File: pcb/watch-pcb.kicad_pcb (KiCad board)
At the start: 4 copper layers, 42 x 42 mm, 71 parts, among them J1 ESP_ANT, J1 USB_C_Receptacle, J2 ESP_ANT, J2 MOTOR, J4 MOTOR, J5 Micro_SD_Card, J6 ESP_ANT, J7 USB_C_Receptacle, Q1 MBT2222ADW1T1, U1 DRV2605LYZFR, U10 APS12808L-3OBMx, U11 LSM6DSV16XTR, U12 ESP32-S3, U13 ADP2108AUJ-1.8, U14 CP2102N-Axx-xQFN28, U16 BQ25638, U17 ADP2108AUJ-1.8, U2 ESP32-S3, U2 TPS63021, U3 BQ25638, U3 TPS63021, U4 TPS65631W, U5 BQ27427YZFR, U5 ESP32-S3, U6 BQ27427YZFR, U6 TCA9535MRGER, U7 MAX30102, U8 LIS3MDL, U9 MX25LM51245GXDI00, Y1 40MHz(10ppm), Y2 32.768kHz, Y3 40MHz(10ppm), Y4 32.768kHz, Y5 40MHz(10ppm), Y6 32.768kHz

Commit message: finished pcb layout
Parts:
- removed BT2: Battery, custom-lib:Battery_Connector
- removed C100, C102: 1.5pF, Capacitor_SMD:C_0201_0603Metric
- removed the D1 at (211.7, 80.8)
- removed the D1 at (130.5, 50.5)
- removed the J1 at (130.2, 48.5)
- removed the J1 at (189.5, 72.8)
- removed the J2 at (205.8, 95.2)
- removed the J2 at (155.0, 42.0)
- removed the J5 at (134.3, 63.6)
- removed the J5 at (176.7, 87.9)
- removed J7: USB_C_Receptacle, Connector_USB:USB_C_Receptacle_GCT_USB4105-xx-A_16P_TopMnt_Horizontal
- removed JP2, JP3, JP4, JP5, JP8: GP6, Jumper:SolderJumper-3_P1.3mm_Open_RoundedPad1.0x1.5mm
- removed JP6, JP7: RESET=LOW, Jumper:SolderJumper-2_P1.3mm_Open_RoundedPad1.0x1.5mm
- removed L13: 2.7nH, Inductor_SMD:L_0201_0603Metric
- removed the MK1 at (204.6, 101.0)
- removed the MK1 at (161.7, 67.0)
- removed R57: R, PCM_Resistor_SMD_AKL:R_0402_1005Metric
- removed the U1 at (199.7, 101.7)
- removed the U1 at (147.5, 76.0)
- removed the U10 at (182.2, 75.1)
- removed the U10 at (147.0, 41.0)
- removed the U11 at (204.6, 105.5)
- removed the U11 at (146.0, 57.0)
- removed U16: BQ25638, custom-lib:Texas_DSBGA-30_2.0x2.4mm_Layout5x6_P0.4mm
- removed U17: ADP2108AUJ-1.8, Package_TO_SOT_SMD:TSOT-23-5
- removed the U2 at (145.5, 62.4)
- removed the U2 at (188.8, 85.0)
- removed the U3 at (207.7, 83.1)
- removed the U3 at (140.7, 55.5)
- removed the U4 at (164.2, 56.6)
- removed the U4 at (209.3, 105.5)
- removed the U5 at (215.2, 82.1)
- removed the U5 at (152.8, 49.0)
- removed the U6 at (127.5, 56.5)
- removed the U6 at (187.3, 92.8)
- removed the U7 at (199.9, 95.8)
- removed the U7 at (146.0, 57.0)
- removed the U8 at (154.2, 59.2)
- removed the U8 at (199.3, 105.7)
- removed the U9 at (173.6, 75.1)
- removed the U9 at (147.0, 41.0)
- removed Y3, Y5: 40MHz(10ppm), Crystal:Crystal_SMD_3225-4Pin_3.2x2.5mm
- removed Y4, Y6: 32.768kHz, Crystal:Crystal_SMD_3215-2Pin_3.2x1.5mm
- added C1: 10uF, Capacitor_SMD:C_0603_1608Metric, B.Cu at (114.3, 83.2)
- added C10: 22uF, Capacitor_SMD:C_0603_1608Metric, F.Cu at (113.2, 76.4)
- added C11: 1uF, Capacitor_SMD:C_0402_1005Metric, F.Cu at (110.3, 53.2)
- added C12: 100nF, Capacitor_SMD:C_0402_1005Metric, B.Cu at (130.7, 78.0)
- added C13: 10uF, Capacitor_SMD:C_0402_1005Metric, B.Cu at (131.7, 78.0)
- added C14: 22uF, Capacitor_SMD:C_0603_1608Metric, B.Cu at (108.3, 56.8)
- added C15: 2.2uF, Capacitor_SMD:C_0402_1005Metric, F.Cu at (113.3, 55.5)
- added C16: 22uF, Capacitor_SMD:C_0603_1608Metric, B.Cu at (110.0, 58.6)
- added C17: 22uF, Capacitor_SMD:C_0603_1608Metric, B.Cu at (106.6, 55.0)
- added C18: 1uF, Capacitor_SMD:C_0402_1005Metric, B.Cu at (108.2, 63.6)
- added C19: 10uF, Capacitor_SMD:C_0402_1005Metric, B.Cu at (107.4, 65.7)
- added C2: 10uF, Capacitor_SMD:C_0603_1608Metric, B.Cu at (114.3, 81.7)
- added C20: 4.7uF, Capacitor_SMD:C_0402_1005Metric, F.Cu at (108.0, 67.8)
- added C21: 4.7uF, Capacitor_SMD:C_0402_1005Metric, F.Cu at (111.7, 64.4)
- added C22: 47nF, Capacitor_SMD:C_0402_1005Metric, F.Cu at (108.7, 66.7)
- added C23: 10uF, Capacitor_SMD:C_0603_1608Metric, B.Cu at (109.9, 62.6)
- added C24: 10uF, Capacitor_SMD:C_0603_1608Metric, B.Cu at (111.4, 62.6)
- added C25: 1.5pF, Capacitor_SMD:C_0201_0603Metric, F.Cu at (121.6, 52.5)
- added C26: 1uF, Capacitor_SMD:C_0402_1005Metric, B.Cu at (120.2, 54.0)
- added C27: C, Capacitor_SMD:C_0402_1005Metric, F.Cu at (114.0, 57.0)
- added C28: C, Capacitor_SMD:C_0402_1005Metric, F.Cu at (114.0, 63.0)
- added C29: 1.5pF, Capacitor_SMD:C_0201_0603Metric, F.Cu at (122.0, 55.5)
- added C3: 4.7uF, Capacitor_SMD:C_0402_1005Metric, B.Cu at (113.7, 59.8)
- added C30: 100nF, Capacitor_SMD:C_0402_1005Metric, B.Cu at (123.0, 67.2)
- added C31: 1uF, Capacitor_SMD:C_0402_1005Metric, F.Cu at (123.2, 72.5)
- added C32: 100nF, Capacitor_SMD:C_0402_1005Metric, B.Cu at (115.7, 59.6)
- added C33: 1uF, Capacitor_SMD:C_0402_1005Metric, F.Cu at (124.8, 55.5)
- added C34: 1uF, Capacitor_SMD:C_0402_1005Metric, B.Cu at (115.0, 63.8)
- added C35: 100nF, Capacitor_SMD:C_0402_1005Metric, F.Cu at (123.8, 61.6)
- added C36: 10nF, Capacitor_SMD:C_0402_1005Metric, F.Cu at (123.5, 55.5)
- added C37: 100nF, Capacitor_SMD:C_0402_1005Metric, B.Cu at (115.0, 64.8)
- added C38: 100nF, Capacitor_SMD:C_0402_1005Metric, B.Cu at (121.3, 56.8)
- added C39: 100nF, Capacitor_SMD:C_0402_1005Metric, B.Cu at (125.3, 54.9)
- added C4: 100nF, Capacitor_SMD:C_0603_1608Metric, B.Cu at (110.3, 78.5)
- added C40: 1uF, Capacitor_SMD:C_0402_1005Metric, B.Cu at (125.5, 53.8)
- added C41: C, Capacitor_SMD:C_0402_1005Metric, F.Cu at (127.3, 56.5)
- added C42: C, Capacitor_SMD:C_0402_1005Metric, F.Cu at (127.2, 61.7)
- added C43: 10uF, Capacitor_SMD:C_0402_1005Metric, B.Cu at (123.8, 53.0)
- added C44: 10uF, Capacitor_SMD:C_0402_1005Metric, B.Cu at (122.5, 53.0)
- added C45: 10uF, Capacitor_SMD:C_0402_1005Metric, B.Cu at (100.9, 80.6)
- added C46: 100nF, Capacitor_SMD:C_0402_1005Metric, F.Cu at (126.7, 63.3)
- added C47: 1uF, Capacitor_SMD:C_0402_1005Metric, F.Cu at (128.9, 62.7)
- added C48: 100nF, Capacitor_SMD:C_0402_1005Metric, B.Cu at (131.2, 58.8)
- added C49: 10uF, Capacitor_SMD:C_0402_1005Metric, F.Cu at (129.9, 58.7)
- added C5: 10nF, Capacitor_SMD:C_0402_1005Metric, B.Cu at (107.3, 62.3)
- added C50: 100nF, Capacitor_SMD:C_0402_1005Metric, F.Cu at (116.3, 84.5)
- added C51: 100nF, Capacitor_SMD:C_0402_1005Metric, B.Cu at (120.3, 86.6)
- added C52: 10uF, Capacitor_SMD:C_0402_1005Metric, F.Cu at (117.3, 84.5)
- added C53: 1uF, Capacitor_SMD:C_0402_1005Metric, B.Cu at (119.2, 87.6)
- added C54: 100nF, Capacitor_SMD:C_0402_1005Metric, F.Cu at (119.5, 72.7)
- added C55: 10uF, Capacitor_SMD:C_0402_1005Metric, F.Cu at (121.0, 73.9)
- added C56: 1uF, Capacitor_SMD:C_0402_1005Metric, B.Cu at (121.7, 91.5)
- added C57: 100nF, Capacitor_SMD:C_0402_1005Metric, F.Cu at (117.6, 69.8)
- added C58: 4.7uF, Capacitor_SMD:C_0402_1005Metric, F.Cu at (117.6, 68.8)
- added C59: 1uF, Capacitor_SMD:C_0402_1005Metric, F.Cu at (119.4, 73.9)
- added C6: 10uF, Capacitor_SMD:C_0402_1005Metric, B.Cu at (111.2, 55.2)
- added C60: 100nF, Capacitor_SMD:C_0402_1005Metric, F.Cu at (115.6, 73.9)
- added C61: 100nF, Capacitor_SMD:C_0402_1005Metric, F.Cu at (117.5, 73.9)
- added C62: 10uF, Capacitor_SMD:C_0402_1005Metric, F.Cu at (114.0, 84.0)
- added C63: 10uF, Capacitor_SMD:C_0402_1005Metric, F.Cu at (117.9, 90.1)
- added C64: 1uF, Capacitor_SMD:C_0402_1005Metric, F.Cu at (108.3, 85.8)
- added C65: 100nF, Capacitor_SMD:C_0402_1005Metric, F.Cu at (109.8, 85.1)
- added C66: 1uF, Capacitor_SMD:C_0402_1005Metric, B.Cu at (114.4, 87.7)
- added C67: 100nF, Capacitor_SMD:C_0402_1005Metric, F.Cu at (114.4, 87.7)
- added C68: 100nF, Capacitor_SMD:C_0402_1005Metric, F.Cu at (99.0, 72.6)
- added C69: 1uF, Capacitor_SMD:C_0402_1005Metric, F.Cu at (100.6, 71.9)
- added C7: 22uF, Capacitor_SMD:C_0603_1608Metric, F.Cu at (113.2, 72.9)
- added C72: 100nF, Capacitor_SMD:C_0402_1005Metric, B.Cu at (108.0, 86.5)
- added C73: 100nF, Capacitor_SMD:C_0402_1005Metric, F.Cu at (109.5, 88.0)
- added C74: 100nF, Capacitor_SMD:C_0402_1005Metric, F.Cu at (132.9, 73.0)
- added C75: 1uF, Capacitor_SMD:C_0402_1005Metric, F.Cu at (131.9, 73.0)
- added C76: 100nF, Capacitor_SMD:C_0402_1005Metric, F.Cu at (129.7, 64.3)
- added C77: 100nF, Capacitor_SMD:C_0402_1005Metric, F.Cu at (128.9, 67.4)
- added C78: 100nF, Capacitor_SMD:C_0402_1005Metric, F.Cu at (125.4, 72.5)
- added C79: 100nF, Capacitor_SMD:C_0402_1005Metric, B.Cu at (123.0, 66.2)
- added C8: 22uF, Capacitor_SMD:C_0603_1608Metric, F.Cu at (113.2, 74.7)
- added C9: 1uF, Capacitor_SMD:C_0402_1005Metric, B.Cu at (133.5, 80.7)
- added D1: STATUS1, LED_SMD:LED_0402_1005Metric, F.Cu at (97.0, 72.6)
- added D10: ESD9B3.3ST5G, Diode_SMD:D_SOD-923, B.Cu at (101.2, 82.0)
- added D11: ESD9B3.3ST5G, Diode_SMD:D_SOD-923, B.Cu at (101.4, 79.1)
- added D12: ESD9B3.3ST5G, Diode_SMD:D_SOD-923, B.Cu at (100.4, 78.7)
- added D13: ESD9B3.3ST5G, Diode_SMD:D_SOD-923, B.Cu at (99.1, 77.8)
- added D14: ESD9B3.3ST5G, Diode_SMD:D_SOD-923, B.Cu at (99.4, 81.7)
- added D15: STATUS0, LED_SMD:LED_0402_1005Metric, F.Cu at (97.4, 68.1)
- added D6: CHARGING, LED_SMD:LED_0402_1005Metric, B.Cu at (105.8, 63.5)
- added D7: POWER GOOD, LED_SMD:LED_0402_1005Metric, B.Cu at (105.8, 64.5)
- added D8: ESD9B3.3ST5G, Diode_SMD:D_SOD-923, B.Cu at (101.2, 84.1)
- added J1: DAUGHTER, Connector_FFC-FPC:TE_1-1734839-2_1x12-1MP_P0.5mm_Horizontal, F.Cu at (133.6, 65.3)
- added J2: USB_C_Receptacle, Connector_USB:USB_C_Receptacle_GCT_USB4105-xx-A_16P_TopMnt_Horizontal, F.Cu at (101.0, 62.8)
- added J3: ESP_ANT, Connector_Coaxial:U.FL_Molex_MCRF_73412-0110_Vertical, F.Cu at (118.5, 53.5)
- added J5: ELV1411A, custom-lib:ELV1411A, F.Cu at (126.8, 81.7)
- added L1: 1.5uH, custom-lib:XFL4020-152ME, F.Cu at (118.0, 76.9)
- added L2: 1uH, Inductor_SMD:L_1206_3216Metric, B.Cu at (113.8, 52.8)
- added L3: 1uH, Inductor_SMD:L_1206_3216Metric, F.Cu at (108.7, 63.6)
- added L4: 2.7nH, Inductor_SMD:L_0201_0603Metric, F.Cu at (121.6, 54.2)
- added L5: 2nH, Inductor_SMD:L_0805_2012Metric, B.Cu at (123.2, 55.9)
- added L6: 24nH, Inductor_SMD:L_Coilcraft_XFL2010, F.Cu at (124.2, 58.0)
- added L8: 10uH, Inductor_SMD:L_1008_2520Metric, B.Cu at (115.2, 89.8)
- added MK1: ICS-43434, Sensor_Audio:InvenSense_ICS-43434-6_3.5x2.65mm, F.Cu at (97.9, 70.4)
- added Q2: MMBT3904, Package_TO_SOT_SMD:SOT-23, B.Cu at (122.6, 81.6)
- added Q3: MMBT3904, Package_TO_SOT_SMD:SOT-23, B.Cu at (126.0, 87.1)
- added Q4: MMBT3904, Package_TO_SOT_SMD:SOT-23, B.Cu at (124.3, 77.8)
- added Q5: MMBT3904, Package_TO_SOT_SMD:SOT-23, B.Cu at (122.6, 85.6)
- added Q6: MMBT3904, Package_TO_SOT_SMD:SOT-23, B.Cu at (118.7, 80.4)
- added R1: 10k, Resistor_SMD:R_0402_1005Metric, F.Cu at (107.8, 28.3)
- added R10: 10k, Resistor_SMD:R_0402_1005Metric, F.Cu at (115.6, 33.9)
- added R11: 5.1k, Resistor_SMD:R_0402_1005Metric, F.Cu at (106.9, 64.0)
- added R12: 5.1k, Resistor_SMD:R_0402_1005Metric, F.Cu at (105.0, 67.4)
- added R13: 180k, Resistor_SMD:R_0402_1005Metric, F.Cu at (110.8, 74.0)
- added R14: 1M, Resistor_SMD:R_0402_1005Metric, F.Cu at (110.2, 72.2)
- added R15: 1M, Resistor_SMD:R_0402_1005Metric, B.Cu at (110.3, 80.7)
- added R16: 22.1k, Resistor_SMD:R_0402_1005Metric, F.Cu at (132.8, 75.7)
- added R17: 47.5k, Resistor_SMD:R_0402_1005Metric, F.Cu at (134.3, 76.8)
- added R18: 1k, Resistor_SMD:R_0402_1005Metric, B.Cu at (133.5, 81.7)
- added R19: 10k, Resistor_SMD:R_0402_1005Metric, F.Cu at (114.8, 52.0)
- added R2: 10k, Resistor_SMD:R_0402_1005Metric, F.Cu at (107.8, 30.3)
- added R20: 0, Resistor_SMD:R_0402_1005Metric, B.Cu at (125.3, 81.0)
- added R22: 30.31, Resistor_SMD:R_0402_1005Metric, B.Cu at (112.8, 63.1)
- added R23: 2222, Resistor_SMD:R_0402_1005Metric, B.Cu at (121.4, 79.1)
- added R24: 10k, Resistor_SMD:R_0402_1005Metric, B.Cu at (125.8, 83.5)
- added R25: 10k, Resistor_SMD:R_0402_1005Metric, B.Cu at (125.3, 80.0)
- added R26: 5.24k, Resistor_SMD:R_0402_1005Metric, B.Cu at (112.8, 65.1)
- added R27: 6666, Resistor_SMD:R_0402_1005Metric, B.Cu at (119.9, 85.1)
- added R28: 0, Resistor_SMD:R_0402_1005Metric, F.Cu at (122.6, 75.7)
- added R29: 0, Resistor_SMD:R_0402_1005Metric, F.Cu at (135.4, 78.3)
- added R3: R, Resistor_SMD:R_0402_1005Metric, F.Cu at (98.0, 73.6)
- added R30: 33k, Resistor_SMD:R_0402_1005Metric, B.Cu at (119.9, 84.1)
- added R31: 10k, Resistor_SMD:R_0402_1005Metric, B.Cu at (121.2, 54.0)
- added R32: 10k, Resistor_SMD:R_0402_1005Metric, B.Cu at (120.7, 55.5)
- added R33: 499, Resistor_SMD:R_0402_1005Metric, B.Cu at (122.9, 60.5)
- added R34: 0, Resistor_SMD:R_0402_1005Metric, F.Cu at (114.3, 65.3)
- added R35: 0, Resistor_SMD:R_0402_1005Metric, F.Cu at (115.3, 65.3)
- added R36: 0, Resistor_SMD:R_0402_1005Metric, F.Cu at (116.3, 65.3)
- added R37: 0, Resistor_SMD:R_0402_1005Metric, F.Cu at (117.3, 65.3)
- added R38: 0, Resistor_SMD:R_0402_1005Metric, F.Cu at (118.3, 65.3)
- added R39: R, PCM_Resistor_SMD_AKL:R_0402_1005Metric, F.Cu at (111.5, 60.0)
- added R4: 10k, Resistor_SMD:R_0402_1005Metric, F.Cu at (107.8, 34.3)
- added R40: 10k, Resistor_SMD:R_0402_1005Metric, F.Cu at (129.3, 69.3)
- added R41: 0, Resistor_SMD:R_0402_1005Metric, B.Cu at (118.9, 64.5)
- added R42: 0, Resistor_SMD:R_0402_1005Metric, B.Cu at (119.9, 64.5)
- added R43: 0, Resistor_SMD:R_0402_1005Metric, B.Cu at (120.9, 64.5)
- added R44: 0, Resistor_SMD:R_0402_1005Metric, B.Cu at (121.9, 64.5)
- added R45: 0, Resistor_SMD:R_0402_1005Metric, F.Cu at (123.9, 63.9)
- added R46: 10k, Resistor_SMD:R_0402_1005Metric, B.Cu at (103.0, 84.1)
- added R47: 10k, Resistor_SMD:R_0402_1005Metric, B.Cu at (102.5, 83.1)
- added R48: 10k, Resistor_SMD:R_0402_1005Metric, B.Cu at (103.0, 82.0)
- added R49: 10k, Resistor_SMD:R_0402_1005Metric, B.Cu at (102.4, 80.2)
- added R5: 10k, Resistor_SMD:R_0402_1005Metric, F.Cu at (107.8, 36.3)
- added R50: 10k, Resistor_SMD:R_0402_1005Metric, B.Cu at (100.4, 76.9)
- added R51: 10k, Resistor_SMD:R_0402_1005Metric, B.Cu at (99.1, 76.0)
- added R52: 10k, Resistor_SMD:R_0402_1005Metric, B.Cu at (134.0, 64.3)
- added R53: 10k, Resistor_SMD:R_0402_1005Metric, F.Cu at (131.2, 58.1)
- added R54: 10k, Resistor_SMD:R_0402_1005Metric, F.Cu at (102.7, 70.7)
- added R55: R, Resistor_SMD:R_0402_1005Metric, F.Cu at (103.9, 69.6)
- added R6: 10k, Resistor_SMD:R_0402_1005Metric, F.Cu at (111.0, 30.9)
- added R7: 10k, Resistor_SMD:R_0402_1005Metric, F.Cu at (111.0, 32.9)
- added R8: 10k, Resistor_SMD:R_0402_1005Metric, F.Cu at (111.0, 34.9)
- added R9: 10k, Resistor_SMD:R_0402_1005Metric, F.Cu at (115.6, 31.9)
- added TH1: 103AT-2 10k, Resistor_THT:R_Axial_DIN0204_L3.6mm_D1.6mm_P2.54mm_Vertical, F.Cu at (113.2, 68.2)
- added TP1: MTP_PWR, TestPoint:TestPoint_Pad_D1.0mm, B.Cu at (112.7, 85.2)
- added U1: ADP2108AUJ-1.8, Package_TO_SOT_SMD:TSOT-23-5, B.Cu at (113.7, 56.4)
- added U10: MAX30102, OptoDevice:Maxim_OLGA-14_3.3x5.6mm_P0.8mm, B.Cu at (116.8, 71.8)
- added U11: TPS65631W, Package_SON:WSON-10-1EP_2.5x2.5mm_P0.5mm_EP1.2x2mm_ThermalVias, F.Cu at (117.5, 87.5)
- added U2: TPS63021, custom-lib:Texas_VSON-14_3x4mm_ThermalPad, B.Cu at (114.2, 78.9)
- added U3: CP2102N-Axx-xQFN28, Package_DFN_QFN:QFN-28-1EP_5x5mm_P0.5mm_EP3.35x3.35mm, B.Cu at (129.4, 82.1)
- added U4: BQ27427YZFR, Package_BGA:Texas_DSBGA-9_1.4715x1.4715mm_Layout3x3_P0.5mm, F.Cu at (112.5, 53.2)
- added U5: BQ25638, custom-lib:Texas_DSBGA-30_2.0x2.4mm_Layout5x6_P0.4mm, B.Cu at (109.8, 65.7)
- added U6: ESP32-S3, Package_DFN_QFN:QFN-56-1EP_7x7mm_P0.4mm_EP4x4mm_ThermalVias, F.Cu at (118.8, 60.2)
- added U7: MX25LM51245GXDI00, custom-lib:BGA-24_6.0x8.0mm_Layout5x5_P1.0mm, F.Cu at (123.6, 68.2)
- added U8: APS12808L-3OBMx, custom-lib:BGA-24_6.0x8.0mm_Layout5x5_P1.0mm, B.Cu at (128.7, 64.8)
- added U9: TCA9535MRGER, Package_DFN_QFN:VQFN-24-1EP_4x4mm_P0.5mm_EP2.45x2.45mm, B.Cu at (127.8, 58.3)
- C70: value 1.5pF -> 1uF; footprint Capacitor_SMD:C_0201_0603Metric -> Capacitor_SMD:C_0402_1005Metric; moved to B.Cu
- C71: value 1.5pF -> 100nF; footprint Capacitor_SMD:C_0201_0603Metric -> Capacitor_SMD:C_0402_1005Metric
- D2, D3: moved to B.Cu
- D4, D5: value ESD9B3.3ST5G -> ESD9B5.0ST5G
- D9: value ESD9B5.0ST5G -> ESD9B3.3ST5G; moved to B.Cu
- J4: value MOTOR -> Micro_SD_Card; footprint custom-lib:Battery_Connector -> Connector_Card:microSD_HC_Hirose_DM3D-SF
- J6: value ESP_ANT -> TT143AMC12C; footprint Connector_Coaxial:U.FL_Molex_MCRF_73412-0110_Vertical -> custom-lib:OK-14GF024-04
- JP1: value BOOT -> RESET=LOW; moved to F.Cu
- L7: value 2.7nH -> 10uH; footprint Inductor_SMD:L_0201_0603Metric -> Inductor_SMD:L_1008_2520Metric; moved to B.Cu
- Q1: value MBT2222ADW1T1 -> MMBT3904; footprint Package_TO_SOT_SMD:SOT-363_SC-70-6 -> Package_TO_SOT_SMD:SOT-23; moved to B.Cu
- R21: value R -> 0; footprint PCM_Resistor_SMD_AKL:R_0402_1005Metric -> Resistor_SMD:R_0402_1005Metric; moved to B.Cu
- U12: value ESP32-S3 -> DRV2605LYZFR; footprint Package_DFN_QFN:QFN-56-1EP_7x7mm_P0.4mm_EP4x4mm_ThermalVias -> Package_BGA:Texas_DSBGA-9_1.4715x1.4715mm_Layout3x3_P0.5mm; moved to B.Cu
- U13: value ADP2108AUJ-1.8 -> LSM6DSV16XTR; footprint Package_TO_SOT_SMD:TSOT-23-5 -> Package_LGA:LGA-14_3x2.5mm_P0.5mm_LayoutBorder3x4y
- U14: value CP2102N-Axx-xQFN28 -> LIS3MDL; footprint Package_DFN_QFN:QFN-28-1EP_5x5mm_P0.5mm_EP3.35x3.35mm -> Package_LGA:LGA-12_2x2mm_P0.5mm
- Y1: value 40MHz(10ppm) -> 32.768kHz; footprint Crystal:Crystal_SMD_3225-4Pin_3.2x2.5mm -> Crystal:Crystal_SMD_3215-2Pin_3.2x1.5mm
- Y2: value 32.768kHz -> 40MHz(10ppm); footprint Crystal:Crystal_SMD_3215-2Pin_3.2x1.5mm -> Crystal:Crystal_SMD_3225-4Pin_3.2x2.5mm
- moved D9 111.0 mm to (100.7, 83.1)
- moved D3 109.5 mm to (104.3, 63.2), turned to -90 degrees
- moved D2 107.6 mm to (105.4, 65.6), turned to 180 degrees
- moved U14 106.4 mm to (107.5, 88.5), turned to 180 degrees
- moved C71 103.3 mm to (105.5, 88.0), turned to -90 degrees
- moved C70 102.3 mm to (106.8, 86.5), turned to -90 degrees
- moved J4 96.0 mm to (104.7, 78.8), turned to -60 degrees
- moved D4 93.6 mm to (105.9, 65.1), turned to 90 degrees
- moved D5 92.9 mm to (106.2, 55.0)
- moved L7 90.2 mm to (117.5, 84.5), turned to -90 degrees
- moved J6 80.4 mm to (111.9, 88.1), turned to -90 degrees
- moved MK2 78.4 mm to (135.5, 73.7), turned to 90 degrees
- moved U12 77.7 mm to (121.4, 89.3)
- moved U13 75.0 mm to (116.8, 71.8)
- moved Q1 73.0 mm to (134.3, 78.3), turned to -90 degrees
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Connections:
- BT1 pad 1: /BAT+ -> +BATT
- C70 pad 1: Net-(J6-In) -> GND
- C70 pad 2: GND -> +3V3
- C71 pad 1: /ESP_ANT -> GND
- C71 pad 2: GND -> +3V3
- D4 pad 2: /USB_DP -> /USB and Power/USB_DM
- D5 pad 2: /USB_DM -> +BATT
- D9 pad 2: /USB and Power/USB_DM -> /MCU and Memory/SD_D3
- J4 pad 1: /MTR_P -> /MCU and Memory/SD_D2
- J4 pad 2: /MTR_M -> /MCU and Memory/SD_D3
- J6 pad 1: Net-(J6-In) -> +3V3
- J6 pad 2: GND -> /IO/TP_INT
- JP1 pad 2: /I2C0_SCL -> /MCU and Memory/EN
- L7 pad 1: Net-(J6-In) -> GND
- L7 pad 2: /ESP_ANT -> Net-(U11-SWN)
- MK2 pad 2: GND -> +3V3
- Q1 pad 1: /USB and Power/RTS -> Net-(Q1-B)
- Q1 pad 2: Net-(Q1A-B1) -> GND
- R21 pad 1: /RTC_P -> Net-(U3-RXD)
- R21 pad 2: /RTC_N -> /MCU and Memory/TX
- U13 pad 1: VBUS -> GND
- U13 pad 2: GND -> /IO/IMU_SDA
- U13 pad 3: VBUS -> /IO/IMU_SCL
- U13 pad 4: +1V8 -> /IO/IMU_INT1
- U13 pad 5: Net-(U13-SW) -> +3V3
- U14 pad 1: unconnected-(U14-~{DCD}-Pad1) -> /IO/IMU_SCL
- U14 pad 10: unconnected-(U14-NC-Pad10) -> +3V3
- U14 pad 11: unconnected-(U14-~{SUSPEND}-Pad11) -> /IO/IMU_SDA
- U14 pad 12: unconnected-(U14-SUSPEND-Pad12) -> GND
- U14 pad 2: unconnected-(U14-~{RI}/CLK-Pad2) -> GND
- U14 pad 4: /USB and Power/USB_DP -> Net-(U14-C1)
- U14 pad 5: /USB and Power/USB_DM -> +3V3
- U14 pad 7: +3V3 -> /IO/MAG_INT
- U14 pad 8: Net-(U14-VBUS) -> /IO/MAG_DRDY
- U14 pad 9: Net-(U14-~{RST}) -> GND
- Y1 pad 1: /CLK_P -> /MCU and Memory/RTC_N
- Y1 pad 2: GND -> /MCU and Memory/RTC_P
- Y2 pad 1: /RTC_N -> Net-(C41-Pad1)
- Y2 pad 2: /RTC_P -> GND
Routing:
- added copper zone on B.Cu, net GND
- added copper zone on F.Cu, net GND
- added copper zone on In1.Cu, net GND
- added copper zone on In2.Cu, net GND
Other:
- outline, holes or cut-outs redrawn

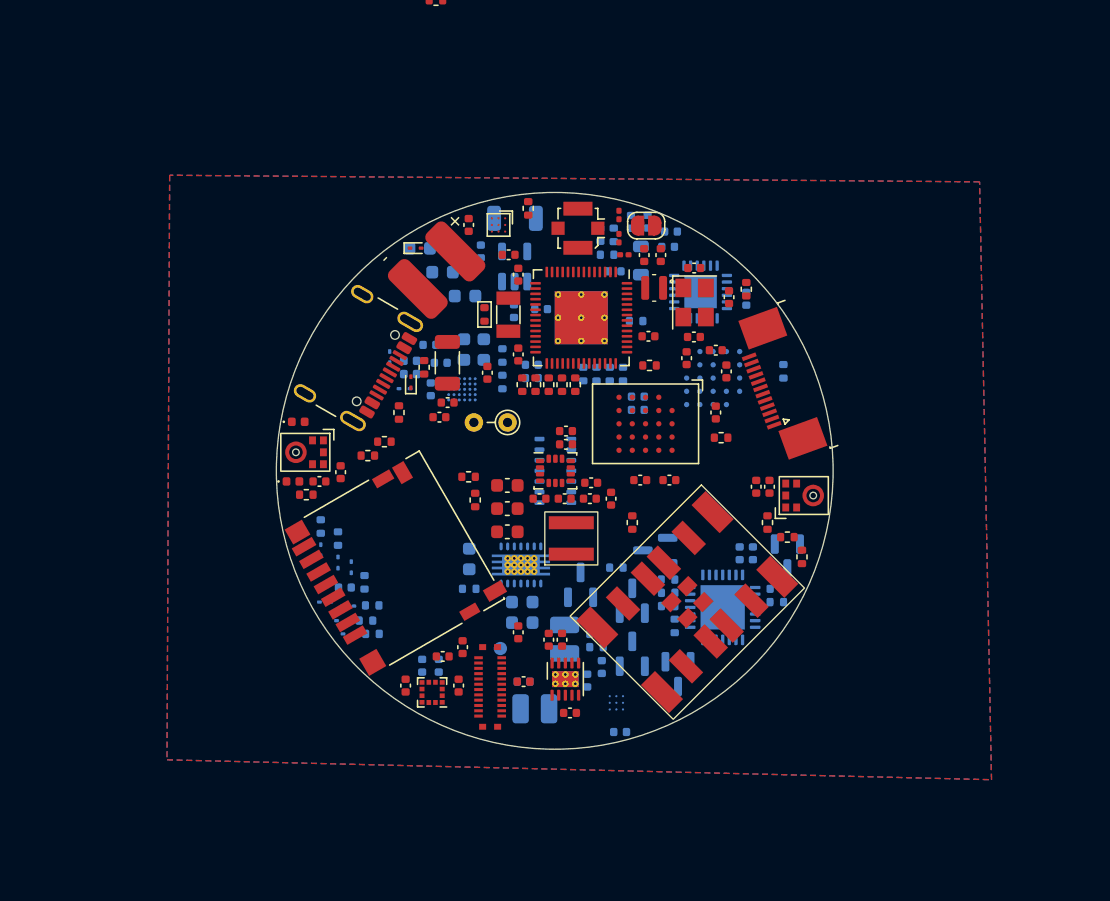
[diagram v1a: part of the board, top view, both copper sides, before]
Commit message: switching to 6 layer
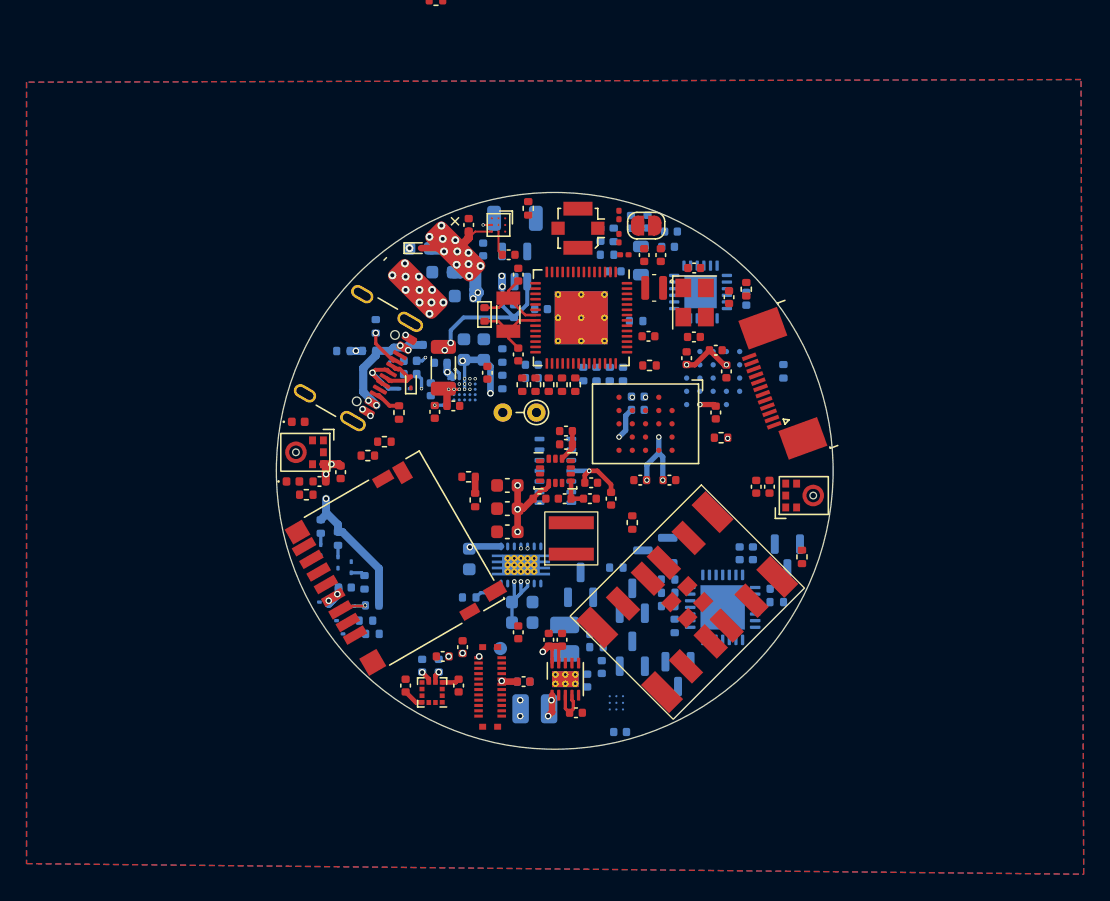
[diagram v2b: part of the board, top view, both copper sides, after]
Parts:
- R11, R16, R17: moved to B.Cu
- moved R17 36.3 mm to (100.8, 62.8), turned to 0 degrees
- moved R16 32.7 mm to (102.8, 62.8), turned to 0 degrees
- moved R11 4.78 mm to (103.2, 60.9), turned to 90 degrees
- moved TH1 2.31 mm to (115.4, 67.4)
- moved R15 0.65 mm to (110.3, 81.3)
- moved C20 0.53 mm to (107.7, 67.3), turned to 90 degrees
- moved C22 0.50 mm to (109.1, 66.9)
- moved L3 0.48 mm to (108.3, 64.0)
- moved C63 0.45 mm to (118.3, 90.0)
- moved C6 0.23 mm to (111.3, 55.1)
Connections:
- net /USB and Power/USB_DM renamed /USB and Power/USB_DN
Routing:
- net +3V3: track 0.00 -> 72.2 mm, vias 0 -> 28
- net +VSW: track 0.00 -> 54.5 mm, vias 0 -> 14
- net +BATT: track 0.00 -> 29.3 mm, vias 0 -> 17
- net VBUS: track 0.00 -> 19.6 mm, vias 0 -> 5
- net /MCU and Memory/RTC_P: track 0.00 -> 6.28 mm
- net /MCU and Memory/RTC_N: track 0.00 -> 6.09 mm
- net /USB and Power/USB_DP: track 0.00 -> 5.48 mm, vias 0 -> 1
- net +1V8: track 0.00 -> 5.05 mm, vias 0 -> 1
- net Net-(D7-K): track 0.00 -> 4.25 mm, vias 0 -> 2
- net Net-(D6-K): track 0.00 -> 4.22 mm, vias 0 -> 2
- net /USB and Power/USB_DN: track 0.00 -> 3.70 mm
- net /IO/AMOLED_P: track 0.00 -> 2.94 mm
- net Net-(J2-CC1): track 0.00 -> 2.90 mm, vias 0 -> 1
- net /MCU and Memory/SD_CMD: track 0.00 -> 2.87 mm, vias 0 -> 1
- net Net-(C22-Pad2): track 0.00 -> 2.63 mm, vias 0 -> 3
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
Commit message: made many changes, maybe switching to stm tho
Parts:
- removed C34: 1uF, Capacitor_SMD:C_0402_1005Metric
- removed C37: 100nF, Capacitor_SMD:C_0402_1005Metric
- removed TP1: MTP_PWR, TestPoint:TestPoint_Pad_D1.0mm
- added R56: R, Resistor_SMD:R_0402_1005Metric, B.Cu at (101.2, 59.8)
- added R57: R, Resistor_SMD:R_0402_1005Metric, B.Cu at (108.1, 61.2)
- D4: moved to B.Cu
- TH1: footprint Resistor_THT:R_Axial_DIN0204_L3.6mm_D1.6mm_P2.54mm_Vertical -> Resistor_SMD:R_0603_1608Metric
- moved D6 6.69 mm to (99.2, 62.8), turned to 150 degrees
- moved D7 6.64 mm to (100.2, 61.1), turned to 150 degrees
- moved D4 2.70 mm to (103.3, 64.4)
- moved TH1 2.61 mm to (112.9, 66.5), turned to 90 degrees
- moved C30 2.50 mm to (123.1, 64.7), turned to 90 degrees
- moved R17 2.09 mm to (102.3, 61.3), turned to -90 degrees
- moved C77 1.50 mm to (130.2, 66.8), turned to 0 degrees
- moved R28 1.31 mm to (123.6, 74.8), turned to 0 degrees
- moved C48 1.18 mm to (130.4, 58.0), turned to 180 degrees
- moved C42 0.95 mm to (128.2, 61.7), turned to 180 degrees
- moved U9 0.92 mm to (126.8, 58.1)
- moved C31 0.61 mm to (122.6, 72.6)
- moved R42 0.56 mm to (119.9, 65.1)
- moved R43 0.56 mm to (120.9, 65.1)
- moved C78 0.56 mm to (124.8, 72.6)
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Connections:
- C32 pad 2: Net-(U6-VDD3P3_CPU) -> +3V3
- C35 pad 2: Net-(U6-VDD3P3_CPU) -> +3V3
- D6 pad 2: +VSW -> Net-(D6-A)
- D7 pad 2: +VSW -> Net-(D7-A)
- J6 pad 24: Net-(J6-MTP_PWR) -> GND
- U6 pad 12: /IO/DISP_RST -> /IO/HBT_INT
- U6 pad 20: Net-(U6-VDD3P3_CPU) -> +3V3
- U6 pad 29: Net-(U6-VDD_SPI) -> unconnected-(U6-VDD_SPI-Pad29)
- U6 pad 36: /MCU and Memory/SD_CLK -> /MCU and Memory/SD_D1
- U6 pad 37: /MCU and Memory/SD_CMD -> /MCU and Memory/SD_D0
- U6 pad 44: /MCU and Memory/SD_D0 -> /MCU and Memory/SD_D2
- U6 pad 45: /MCU and Memory/SD_D1 -> /MCU and Memory/SD_D3
- U6 pad 46: Net-(U6-VDD3P3_CPU) -> +3V3
- U6 pad 47: /MCU and Memory/SD_D2 -> /MCU and Memory/SD_CMD
- U6 pad 48: /MCU and Memory/SD_D3 -> /MCU and Memory/SD_CLK
- U9 pad 4: /IO/HBT_INT -> /IO/DISP_RST
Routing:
- net +3V3: track 72.2 -> 217.1 mm, vias 28 -> 39
- net Net-(Q1-B): track 0.93 -> 43.7 mm, vias 1 -> 2
- net /MCU and Memory/EN: track 0.00 -> 39.2 mm, vias 0 -> 2
- net /MCU and Memory/EXT_IO14: track 2.56 -> 37.2 mm, vias 0 -> 4
- net /IO/MAG_DRDY: track 0.00 -> 33.0 mm, vias 0 -> 2
- net /MCU and Memory/SD_D3: track 0.87 -> 33.5 mm, vias 0 -> 3
- net /USB and Power/USB_DN: track 3.70 -> 36.3 mm, vias 0 -> 2
- net /MCU and Memory/SD_CLK: track 1.09 -> 33.6 mm, vias 0 -> 2
- net /MCU and Memory/SD_D2: track 0.87 -> 33.3 mm, vias 0 -> 3
- net /IO/MAG_INT: track 0.00 -> 32.3 mm, vias 0 -> 2
- net /USB and Power/ILIM: track 0.00 -> 31.9 mm, vias 0 -> 6
- net /MCU and Memory/SD_CMD: track 2.87 -> 33.9 mm, vias 1 -> 3
- net /IO/MIC_SD: track 0.00 -> 29.9 mm, vias 0 -> 3
- net /MCU and Memory/SD_D0: track 0.88 -> 29.4 mm, vias 0 -> 2
- net +1V8: track 5.05 -> 33.3 mm, vias 1 -> 2
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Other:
- board size 42 x 42 mm -> 43 x 43 mm
- copper layers 4 -> 6

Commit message: things
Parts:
- removed C25, C29: 1.5pF, Capacitor_SMD:C_0201_0603Metric
- removed J3: ESP_ANT, Connector_Coaxial:U.FL_Molex_MCRF_73412-0110_Vertical
- removed L4: 2.7nH, Inductor_SMD:L_0201_0603Metric
- removed U6: ESP32-S3, Package_DFN_QFN:QFN-56-1EP_7x7mm_P0.4mm_EP4x4mm_ThermalVias
- added U15: STM32H7S7A8I6, Package_BGA:UFBGA-169_7x7mm_Layout13x13_P0.5mm, F.Cu at (132.2, 49.9)
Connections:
- R33 pad 2: Net-(U6-U0TXD) -> unconnected-(R33-Pad2)
- R34 pad 2: Net-(U6-SPIHD) -> unconnected-(R34-Pad2)
- R35 pad 2: Net-(U6-SPIWP) -> unconnected-(R35-Pad2)
- R36 pad 2: Net-(U6-SPICLK) -> unconnected-(R36-Pad2)
- R37 pad 2: Net-(U6-SPIQ) -> unconnected-(R37-Pad2)
- R38 pad 2: Net-(U6-SPID) -> unconnected-(R38-Pad2)
- R41 pad 2: Net-(U6-GPIO33) -> unconnected-(R41-Pad2)
- R42 pad 2: Net-(U6-GPIO34) -> unconnected-(R42-Pad2)
- R43 pad 2: Net-(U6-GPIO35) -> unconnected-(R43-Pad2)
- R44 pad 2: Net-(U6-GPIO36) -> unconnected-(R44-Pad2)
- R45 pad 2: Net-(U6-GPIO37) -> unconnected-(R45-Pad2)
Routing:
- net (no net): track 0.00 -> 5.29 mm
- net unconnected-(R34-Pad2): track 0.00 -> 3.14 mm
- net Net-(U6-SPIHD): track 3.14 -> 0.00 mm
- net Net-(J3-In): track 2.88 -> 0.00 mm
- net unconnected-(R35-Pad2): track 0.00 -> 2.72 mm
- net Net-(U6-SPIWP): track 2.72 -> 0.00 mm
- net /MCU and Memory/ESP_ANT: track 2.40 -> 0.00 mm
- net unconnected-(R36-Pad2): track 0.00 -> 2.40 mm
- net Net-(U6-SPICLK): track 2.40 -> 0.00 mm
- net unconnected-(R45-Pad2): track 0.00 -> 2.10 mm
- net Net-(U6-GPIO37): track 2.10 -> 0.00 mm
- net unconnected-(R37-Pad2): track 0.00 -> 1.94 mm
- net Net-(U6-SPIQ): track 1.94 -> 0.00 mm
- net unconnected-(R38-Pad2): track 0.00 -> 1.69 mm
- net Net-(U6-SPID): track 1.69 -> 0.00 mm
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
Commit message: what i said before
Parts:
- removed C19: 10uF, Capacitor_SMD:C_0402_1005Metric
- removed C20, C21: 4.7uF, Capacitor_SMD:C_0402_1005Metric
- removed C22: 47nF, Capacitor_SMD:C_0402_1005Metric
- removed C23, C24: 10uF, Capacitor_SMD:C_0603_1608Metric
- removed L3: 1uH, Inductor_SMD:L_1206_3216Metric
- removed Q1, Q2, Q3, Q4, Q5, Q6: MMBT3904, Package_TO_SOT_SMD:SOT-23
- removed R17: 47.5k, Resistor_SMD:R_0402_1005Metric
- removed R18: 1k, Resistor_SMD:R_0402_1005Metric
- removed R20, R21, R28, R29: 0, Resistor_SMD:R_0402_1005Metric
- removed R22: 30.31, Resistor_SMD:R_0402_1005Metric
- removed R23: 2222, Resistor_SMD:R_0402_1005Metric
- removed R24, R25: 10k, Resistor_SMD:R_0402_1005Metric
- removed R26: 5.24k, Resistor_SMD:R_0402_1005Metric
- removed R27: 6666, Resistor_SMD:R_0402_1005Metric
- removed R30: 33k, Resistor_SMD:R_0402_1005Metric
- removed TH1: 103AT-2 10k, Resistor_SMD:R_0603_1608Metric
- removed U15: STM32H7S7A8I6, Package_BGA:UFBGA-169_7x7mm_Layout13x13_P0.5mm
- removed U5: BQ25638, custom-lib:Texas_DSBGA-30_2.0x2.4mm_Layout5x6_P0.4mm
- added C88: 4.7uF, Capacitor_SMD:C_0402_1005Metric, F.Cu at (147.0, 69.2)
- added C89: 10uF, Capacitor_SMD:C_0402_1005Metric, F.Cu at (147.0, 71.2)
- added C90: 10uF, Capacitor_SMD:C_0402_1005Metric, F.Cu at (147.0, 73.2)
- added IC1: APS256XXN-OBR-BG, custom-lib:BGA-24_6.0x8.0mm_Layout5x5_P1.0mm, F.Cu at (130.1, 46.7)
- added R60: 30.1, Resistor_SMD:R_0402_1005Metric, F.Cu at (144.1, 69.2)
- added R61: 5.32k, Resistor_SMD:R_0402_1005Metric, F.Cu at (144.1, 71.2)
- added R62: 5k, Resistor_SMD:R_0402_1005Metric, F.Cu at (144.1, 73.2)
- added TH2: 103AT-2 10k, Resistor_SMD:R_0603_1608Metric, F.Cu at (149.7, 64.9)
- added U6: BQ25628E, custom-lib:Texas_WQFN-18_2.5x3.0mm_P0.4mm, F.Cu at (145.2, 66.0)
- added Y3: 32.768kHz, Crystal:Crystal_SMD_3215-2Pin_3.2x1.5mm, F.Cu at (153.8, 52.8)
- C14: value 22uF -> 1uF; footprint Capacitor_SMD:C_0603_1608Metric -> Capacitor_SMD:C_0402_1005Metric
- C16: value 22uF -> 47nF; footprint Capacitor_SMD:C_0603_1608Metric -> Capacitor_SMD:C_0402_1005Metric
- C17: value 22uF -> 100nF; footprint Capacitor_SMD:C_0603_1608Metric -> Capacitor_SMD:C_0402_1005Metric
- U3: value CP2102N-Axx-xQFN28 -> STM32H7S7L8H6H; footprint Package_DFN_QFN:QFN-28-1EP_5x5mm_P0.5mm_EP3.35x3.35mm -> Package_BGA:ST_TFBGA-225_13x13mm_Layout15x15_P0.8mm; moved to F.Cu
- moved U3 47.9 mm to (128.4, 34.2), turned to 0 degrees
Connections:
- C14 pad 1: +BATT -> VBUS
- C16 pad 1: +BATT -> Net-(U6-BTST)
- C16 pad 2: GND -> Net-(U6-SW)
- C17 pad 1: +BATT -> Net-(U6-PMID)
- R56 pad 1: Net-(D7-A) -> Net-(D6-A)
- R56 pad 2: +VSW -> +3V3
- R57 pad 1: Net-(D6-A) -> Net-(D7-A)
- R57 pad 2: +VSW -> +3V3
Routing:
- net (no net): track 5.29 -> 59.8 mm, vias 0 -> 14
- net /MCU and Memory/RX: track 18.6 -> 0.00 mm, vias 3 -> 0
- net unconnected-(U3A-PC8-PadD15): track 0.00 -> 14.6 mm, vias 0 -> 2
- net Net-(Q3-C): track 14.6 -> 0.00 mm, vias 2 -> 0
- net Net-(Q4-B): track 13.6 -> 0.00 mm, vias 2 -> 0
- net unconnected-(U3A-PM11-PadB7): track 0.00 -> 13.0 mm, vias 0 -> 2
- net Net-(Q4-C): track 12.8 -> 0.00 mm, vias 2 -> 0
- net Net-(Q3-B): track 6.82 -> 0.00 mm
- net Net-(Q6-C): track 5.35 -> 0.00 mm
- net Net-(U5-TS_BIAS): track 2.65 -> 0.00 mm
- net Net-(C22-Pad2): track 2.21 -> 0.00 mm, vias 3 -> 0
- net Net-(Q2-C): track 1.85 -> 0.00 mm
- net Net-(C19-Pad2): track 1.78 -> 0.00 mm
- net Net-(U5-REGN): track 1.22 -> 0.00 mm, vias 3 -> 0
- net Net-(U5-BTST): track 0.68 -> 0.00 mm, vias 1 -> 0
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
